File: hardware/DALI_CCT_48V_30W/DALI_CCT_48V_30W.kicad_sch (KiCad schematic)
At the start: 82 parts, among them J1 Phoenix 5.08mm 2-pin 48V_IN, J2 DALI_A/DALI_B Phoenix 5.08mm, J3 LED+/WW-/CW- Phoenix 5.08mm, J4 SWD 1.27mm 4-pin (GND/SWDIO/S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, Q1 AON7534 N-ch 30V 25A, Q2 AON7534 N-ch 30V 25A, Q3 AON6424 N-ch 40V 20A, Q4 AON6424 N-ch 40V 20A

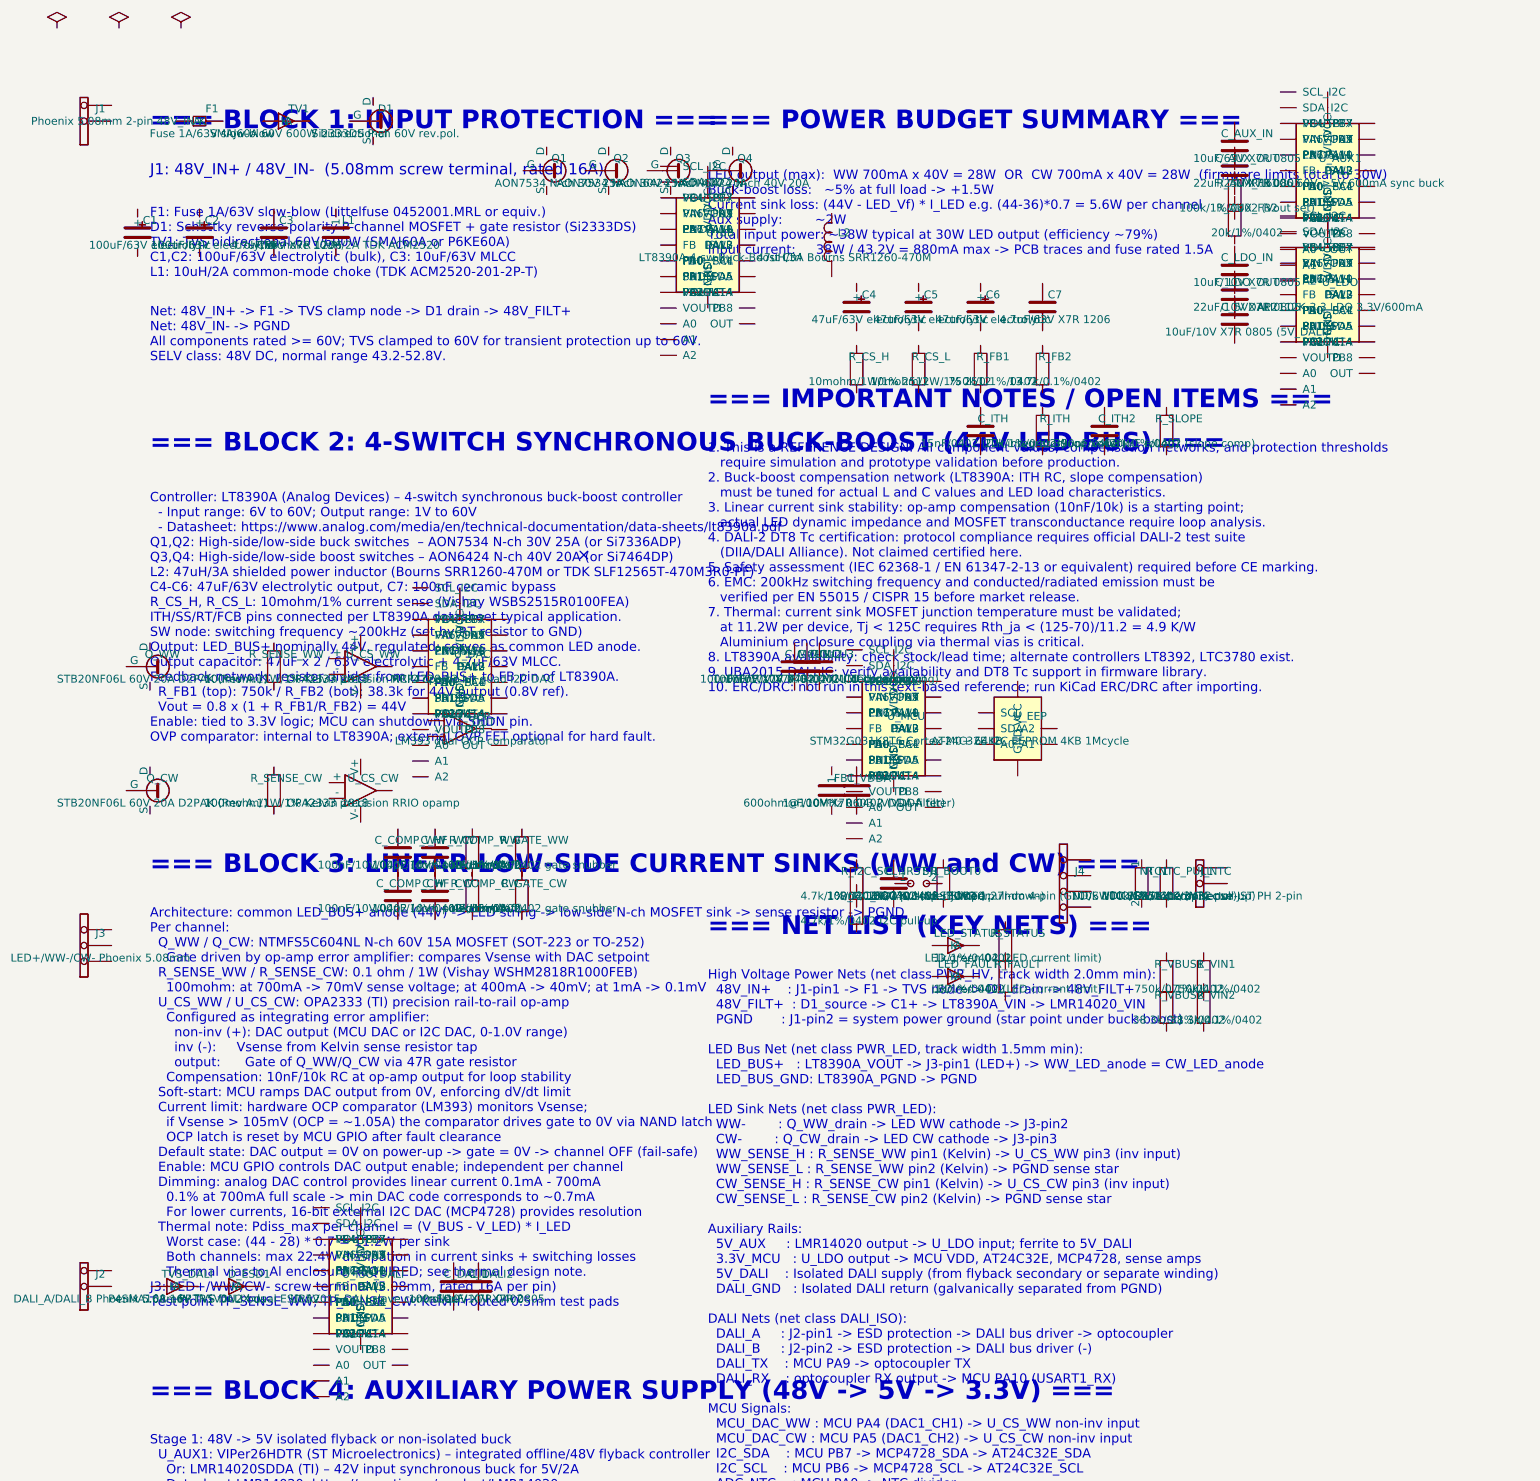
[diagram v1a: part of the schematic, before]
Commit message: Complete schematic wiring: 227 net labels, 101 no_connect markers across 60 nets (OI-011 resolved)
Co-authored-by: manuelh83 <208121220+manuelh83@users.noreply.github.com>
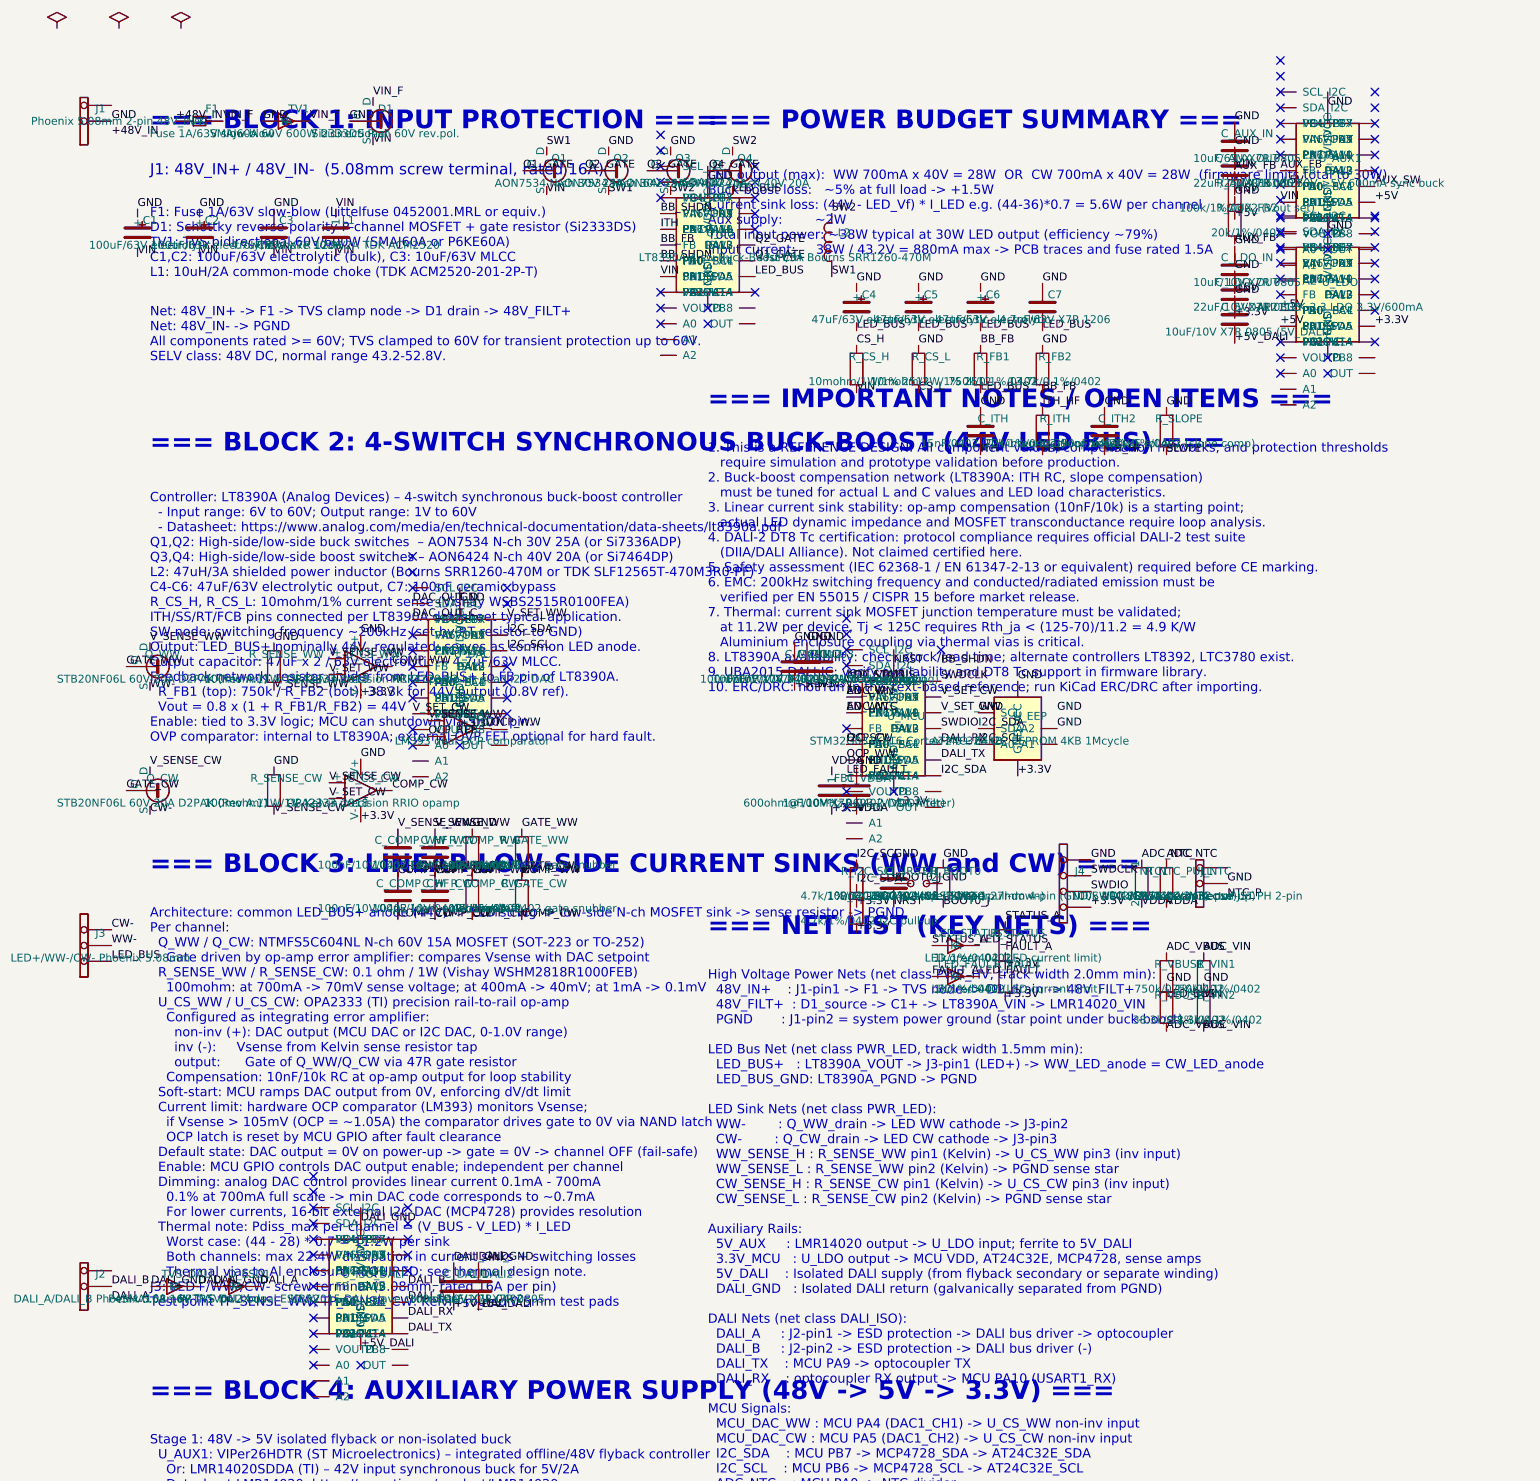
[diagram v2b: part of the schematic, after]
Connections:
- net GND: now reaches C7.1
- net GND: now also C1.+, C2.+, C3.1, C4.+, C5.+, C6.+, C_5VDALI.1, C_AUX_IN.1, C_AUX_OUT.1, C_ITH.1, C_ITH2.1, C_LDO_IN.1, C_LDO_OUT.1, C_MCU1.1, C_MCU2.1, C_MCU3.1, C_NRST.1, C_VDDA.1, D1.G, J1.2 (Pin_2), J4.1 (Pin_1), J_NTC.2 (Pin_2), Q2.D, Q3.D, R_AUX_FB2.1, R_BOOT0.1, R_COMP_CW.1, R_COMP_WW.1, R_CS_L.1, R_FB2.1, R_SENSE_CW.1, R_SENSE_WW.1, R_SLOPE.1, R_VBUS2.1, R_VIN2.1, SJ1.2, TV1.A, U_AUX1.VDD, U_BB.VDD, U_CS_CW.V+, U_CS_WW.V+, U_DAC.VDD, U_EEP.A2, U_EEP.SCL, U_EEP.VCC, U_LDO.VDD
- net LED_BUS: now reaches C7.2
- net LED_BUS: now also C4.-, C5.-, C6.-, J3.3 (Pin_3), Q4.S, R_FB1.2, R_VBUS1.2, U_BB.PA5, U_BB.SDA
- net ADC_VIN: now reaches R_VIN2.2
- net ADC_VIN: now also R_VIN1.1, U_MCU.PA6, U_MCU.VIN
- net +5V: now reaches C_LDO_IN.2
- net +5V: now also C_AUX_OUT.2, R_AUX_FB1.2, U_AUX1.ITH, U_AUX1.PA0, U_AUX1.PA5, U_AUX1.PB0, U_AUX1.SDA, U_LDO.ITH, U_LDO.PA0, U_LDO.PA1, U_LDO.PB0, U_LDO.PB1, U_LDO.SHDN
- net V_SENSE_WW: now reaches R_SENSE_WW.2
- net V_SENSE_WW: now also C_COMP_WW.1, C_HF_WW.1, Q_WW.D, U_CS_WW.+, U_OCP.+
- net COMP_WW: now reaches C_HF_WW.2
- net COMP_WW: now also C_COMP_WW.2, R_COMP_WW.2, R_GATE_WW.2, U_CS_WW.~
- net ITH_HF: now reaches C_ITH2.2
- net ITH_HF: now also R_ITH.1
- net I2C_SCL: now reaches U_DAC.DALI+, U_DAC.PA10, U_DAC.SW1
- net I2C_SCL: now also R_I2C_SCL.1, U_EEP.A0, U_MCU.ITH, U_MCU.PA0, U_MCU.PB0
- net +3.3V: now reaches U_DAC.GND, U_DAC.NRST
- net +3.3V: now also C_LDO_OUT.2, C_MCU1.2, C_MCU2.2, C_MCU3.2, FB1.2, J4.4 (Pin_4), R_FAULT.2, R_I2C_SCL.2, R_I2C_SDA.2, R_STATUS.2, U_CS_CW.V-, U_CS_WW.V-, U_EEP.GND, U_LDO.PA5, U_LDO.SDA
- net V_SET_CW: now reaches U_DAC.PA2, U_DAC.PB3, U_DAC.VOUTC
- net V_SET_CW: now also U_CS_CW.-, U_MCU.PA9, U_MCU.RX, U_MCU.VOUT
- net I2C_SDA: now reaches U_DAC.PA9, U_DAC.RX, U_DAC.VOUT
- net I2C_SDA: now also R_I2C_SDA.1, U_EEP.SDA, U_MCU.PA14, U_MCU.VOUTA
- net DAC_OUT_C: now reaches U_DAC.PB4, U_DAC.VOUTB
- net V_SET_WW: now reaches U_DAC.PB7, U_DAC.TX
- net V_SET_WW: now also U_CS_WW.-, U_MCU.DALI+, U_MCU.PA10, U_MCU.SW1
- net DAC_OUT_D: now reaches U_DAC.SDA_I2C
- net STATUS_A: now reaches R_STATUS.1
- net STATUS_A: now also LED_STATUS.A
- net CW-: now reaches J3.1 (Pin_1)
- net CW-: now also Q_CW.S
- net WW-: now reaches J3.2 (Pin_2)
- net WW-: now also Q_WW.S
- net V_SENSE_CW: now reaches C_HF_CW.1
- net V_SENSE_CW: now also C_COMP_CW.1, Q_CW.D, R_SENSE_CW.2, U_CS_CW.+
- net COMP_CW: now reaches C_HF_CW.2
- net COMP_CW: now also C_COMP_CW.2, R_COMP_CW.2, R_GATE_CW.2, U_CS_CW.~
- net AUX_FB: now reaches R_AUX_FB1.1
- net AUX_FB: now also R_AUX_FB2.2, U_AUX1.FB
- net VIN_F: now reaches D1.D
- net VIN_F: now also F1.K, TV1.K
- net VIN: now reaches D1.S
- net VIN: now also C1.-, C2.-, C3.2, C_AUX_IN.2, L1.1, L1.2, Q1.S, R_CS_H.2, R_VIN1.2, U_AUX1.PA1, U_AUX1.PB1, U_AUX1.SHDN, U_BB.PA1, U_BB.PB1, U_BB.SHDN
- net DALI_GND: now reaches C_DALI1.1
- net DALI_GND: now also C_DALI2.1, D_ESD1.A, TVS_DALI.A, U_ISO_DALI.VDD
- net +5V_DALI: now reaches C_DALI1.2
- net +5V_DALI: now also C_5VDALI.2, C_DALI2.2, U_ISO_DALI.GND, U_ISO_DALI.NRST
- net GATE_CW: now reaches R_GATE_CW.1
- net GATE_CW: now also Q_CW.G
- net Q3_GATE: now reaches Q3.G
- net SW2: now reaches Q3.S
- net SW2: now also L2.1, Q4.D
- net ADC_VBUS: now reaches R_VBUS1.1
- net ADC_VBUS: now also LED_STATUS.K, R_VBUS2.2, U_MCU.PB4, U_MCU.VOUTB
- net Q2_GATE: now reaches U_BB.DALI-, U_BB.PA13, U_BB.SW2
- net Q2_GATE: now also Q2.G
- net ITH: now reaches U_BB.EN, U_BB.PA7, U_BB.PB6
- net ITH: now also C_ITH.2, R_ITH.2
- net BB_FB: now reaches U_BB.FB
- net BB_FB: now also R_FB1.1, R_FB2.2
- net BB_SHDN: now reaches U_BB.ITH, U_BB.PA0, U_BB.PB0
- net BB_SHDN: now also U_BB.PA6, U_BB.VIN
- net Q1_GATE: now reaches U_BB.PA4, U_BB.SCL
- net Q1_GATE: now also Q1.G
- net FAULT_A: now reaches R_FAULT.1
- net FAULT_A: now also LED_FAULT.A
- net GATE_WW: now reaches R_GATE_WW.1
- net GATE_WW: now also Q_WW.G
- net ADC_NTC: now reaches R_NTC_PULL.1
- net ADC_NTC: now also NTC1.1, U_MCU.EN, U_MCU.PA7, U_MCU.PB6
- net VDDA: now reaches R_NTC_PULL.2
- net VDDA: now also C_VDDA.2, FB1.1, NTC1.2
- net CS_H: now reaches R_CS_H.1
- net SLOPE: now reaches R_SLOPE.2
- net SWDCLK: now reaches J4.2 (Pin_2)
- net SWDCLK: now also U_MCU.PB7, U_MCU.TX
- net SWDIO: now reaches J4.3 (Pin_3)
- net SWDIO: now also U_MCU.DALI-, U_MCU.PA13, U_MCU.SW2
- net +48V_IN: now reaches F1.A
- net NRST: now reaches C_NRST.2
- net NRST: now also U_MCU.VDD
- net BOOT0_J: now reaches SJ1.1
- net BOOT0_J: now also R_BOOT0.2
- net OCP_REF: now reaches U_OCP.-
- net OCP_WW: now reaches U_OCP.OUT
- net OCP_WW: now also U_MCU.PA1, U_MCU.PB1, U_MCU.SHDN
- net SW1: now reaches L2.2
- net SW1: now also Q1.D, Q2.S
- net DALI_B: now reaches J2.2 (Pin_2)
- net DALI_B: now also U_ISO_DALI.DALI-, U_ISO_DALI.PA13, U_ISO_DALI.SW2
- net DALI_TX: now reaches U_ISO_DALI.PA14, U_ISO_DALI.VOUTA
- net DALI_TX: now also U_MCU.PA5, U_MCU.SDA
- net DALI_A: now reaches U_ISO_DALI.PA4, U_ISO_DALI.SCL
- net DALI_A: now also D_ESD1.K, TVS_DALI.K
- net DALI_RX: now reaches U_ISO_DALI.PA5, U_ISO_DALI.SDA
- net DALI_RX: now also U_MCU.PA4, U_MCU.SCL
- net LED_FAULT: now reaches LED_FAULT.K
- net LED_FAULT: now also U_MCU.PA2, U_MCU.PB3, U_MCU.VOUTC
- net Q4_GATE: now reaches Q4.G
- net CS_L: now reaches R_CS_L.2
- net AUX_SW: now reaches U_AUX1.PA4, U_AUX1.SCL
- no-connect marks 1 -> 101
